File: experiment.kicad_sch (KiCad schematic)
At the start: 4 parts, among them J3 Laser, J4 PZT, U14 MIC94090YC6

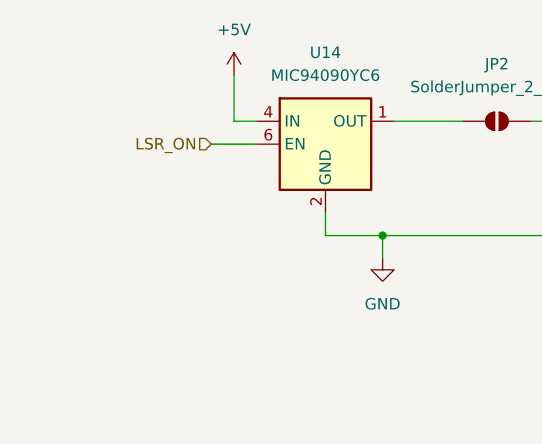
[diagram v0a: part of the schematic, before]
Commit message: Fix review suggestions from non-fpga board
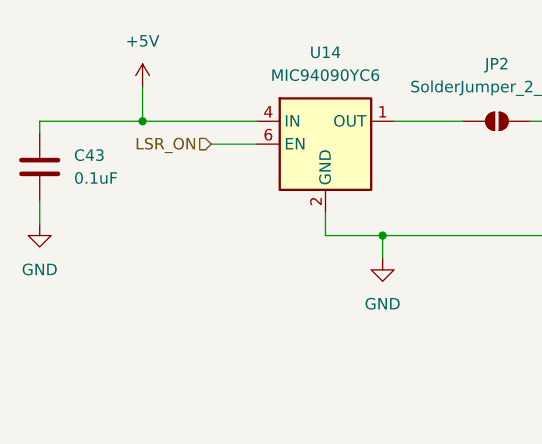
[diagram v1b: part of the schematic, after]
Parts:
- added C43: 0.1uF, Capacitor_SMD:C_0805_2012Metric_Pad1.18x1.45mm_HandSolder, symbol Device:C
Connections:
- net +5V: now also C43.2
- net GND: now also C43.1
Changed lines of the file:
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@@
 	(paper "A4")
+	(junction
+		(at 67.31 64.77)
+		(diameter 0)
+		(color 0 0 0 0)
+	)
 	(junction
 		(at 93.98 77.47)
@@
 	(wire
 		(pts
+			(xy 67.31 60.96) (xy 67.31 64.77)
+		)
+		(stroke
+			(width 0)
+			(type default)
+		)
+	)
+	(wire
+		(pts
 			(xy 96.52 114.3) (xy 96.52 107.95)
 		)
@@
 	(wire
 		(pts
+			(xy 67.31 64.77) (xy 80.01 64.77)
+		)
+		(stroke
+			(width 0)
+			(type default)
+		)
+	)
+	(wire
+		(pts
 			(xy 96.52 107.95) (xy 104.14 107.95)
 		)
@@
 	(wire
 		(pts
+			(xy 55.88 73.66) (xy 55.88 76.2)
+		)
+		(stroke
+			(width 0)
+			(type default)
+		)
+	)
+	(wire
+		(pts
 			(xy 87.63 74.93) (xy 87.63 77.47)
 		)
@@
 	(wire
 		(pts
-			(xy 80.01 64.77) (xy 77.47 64.77)
+			(xy 55.88 64.77) (xy 55.88 66.04)
+		)
+		(stroke
+			(width 0)
+			(type default)
+		)
+	)
+	(wire
+		(pts
+			(xy 55.88 64.77) (xy 67.31 64.77)
 		)
 		(stroke
@@
 		(pts
 			(xy 87.63 77.47) (xy 93.98 77.47)
-		)
-		(stroke
-			(width 0)
-			(type default)
-		)
-	)
-	(wire
-		(pts
-			(xy 77.47 64.77) (xy 77.47 59.69)
 		)
 		(stroke
@@
 	)
 	(symbol
+		(lib_id "power:GND")
+		(at 55.88 76.2 0)
+		(unit 1)
+		(exclude_from_sim no)
+		(in_bom yes)
+		(on_board yes)
+		(dnp no)
+		(fields_autoplaced yes)
+		(property "Reference" "#PWR098"
+			(at 55.88 82.55 0)
+			(effects
+				(font
+					(size 1.27 1.27)
+				)
+				(hide yes)
+			)
+		)
+		(property "Value" "GND"
+			(at 55.88 81.28 0)
+			(effects
+				(font
+					(size 1.27 1.27)
+				)
+			)
+		)
+		(property "Footprint" ""
+			(at 55.88 76.2 0)
+			(effects
+				(font
+					(size 1.27 1.27)
+				)
+				(hide yes)
+			)
+		)
+		(property "Datasheet" ""
+			(at 55.88 76.2 0)
+			(effects
+				(font
+					(size 1.27 1.27)
+				)
+				(hide yes)
+			)
+		)
+		(property "Description" "Power symbol creates a global label with name \"GND\" , ground"
+			(at 55.88 76.2 0)
+			(effects
+				(font
+					(size 1.27 1.27)
+				)
+				(hide yes)
+			)
+		)
+		(pin "1"
+		)
+		(instances
+			(project "FPGA-Lockin"
+				(path "/0d4da0fe-f3e4-47fc-a7f7-d58161fd7b20/40462d7a-51ec-4f16-be35-5e9b22f6b0f0"
+					(reference "#PWR098")
+					(unit 1)
+				)
+			)
+		)
+	)
+	(symbol
+		(lib_id "Device:C")
+		(at 55.88 69.85 180)
+		(unit 1)
+		(exclude_from_sim no)
+		(in_bom yes)
+		(on_board yes)
+		(dnp no)
+		(fields_autoplaced yes)
+		(property "Reference" "C43"
+			(at 59.69 68.5799 0)
+			(effects
+				(font
+					(size 1.27 1.27)
+				)
+				(justify right)
+			)
+		)
+		(property "Value" "0.1uF"
+			(at 59.69 71.1199 0)
+			(effects
+				(font
+					(size 1.27 1.27)
+				)
+				(justify right)
+			)
+		)
+		(property "Footprint" "Capacitor_SMD:C_0805_2012Metric_Pad1.18x1.45mm_HandSolder"
+			(at 54.9148 66.04 0)
+			(effects
+				(font
+					(size 1.27 1.27)
+				)
+				(hide yes)
+			)
+		)
+		(property "Datasheet" "~"
+			(at 55.88 69.85 0)
+			(effects
+				(font
+					(size 1.27 1.27)
+				)
+				(hide yes)
+			)
+		)
+		(property "Description" "Unpolarized capacitor"
+			(at 55.88 69.85 0)
+			(effects
+				(font
+					(size 1.27 1.27)
+				)
+				(hide yes)
+			)
+		)
+		(pin "2"
+		)
+		(pin "1"
+		)
+		(instances
+			(project ""
+				(path "/0d4da0fe-f3e4-47fc-a7f7-d58161fd7b20/40462d7a-51ec-4f16-be35-5e9b22f6b0f0"
+					(reference "C43")
+					(unit 1)
+				)
+			)
+		)
+	)
+	(symbol
 		(lib_id "power:+5V")
-		(at 77.47 59.69 0)
+		(at 67.31 60.96 0)
 		(unit 1)
 		(exclude_from_sim no)
@@
 		(fields_autoplaced yes)
 		(property "Reference" "#PWR067"
-			(at 77.47 63.5 0)
+			(at 67.31 64.77 0)
 			(effects
 				(font
@@
 		)
 		(property "Value" "+5V"
-			(at 77.47 54.61 0)
+			(at 67.31 55.88 0)
 			(effects
 				(font
@@
 		)
 		(property "Footprint" ""
-			(at 77.47 59.69 0)
+			(at 67.31 60.96 0)
 			(effects
 				(font
@@
 		)
 		(property "Datasheet" ""
-			(at 77.47 59.69 0)
+			(at 67.31 60.96 0)
 			(effects
 				(font
@@
 		)
 		(property "Description" "Power symbol creates a global label with name \"+5V\""
-			(at 77.47 59.69 0)
-			(effects
-				(font
+			(at 67.31 60.96 0)
+			(effects
+				(font

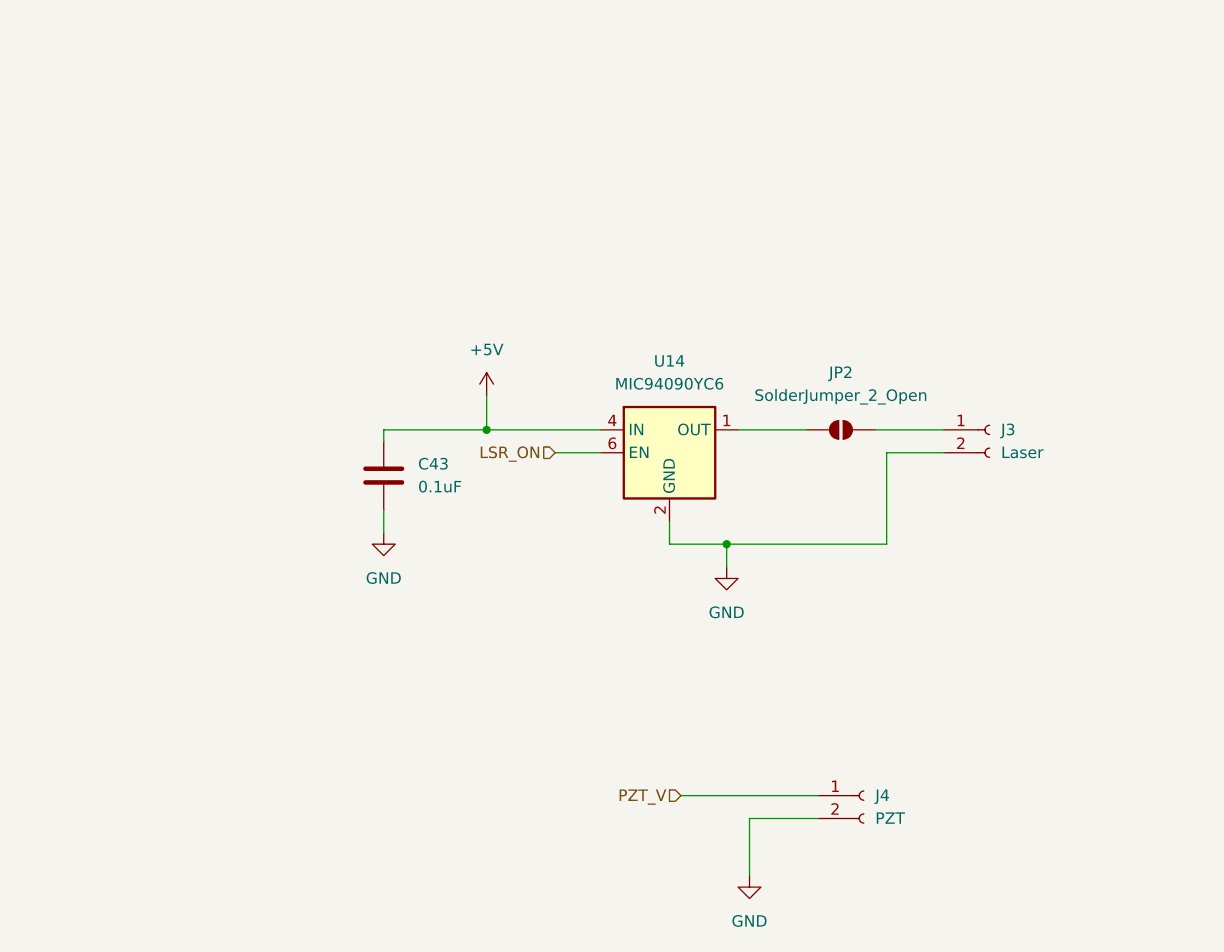
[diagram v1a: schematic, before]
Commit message: Fix everything based on component availabilty
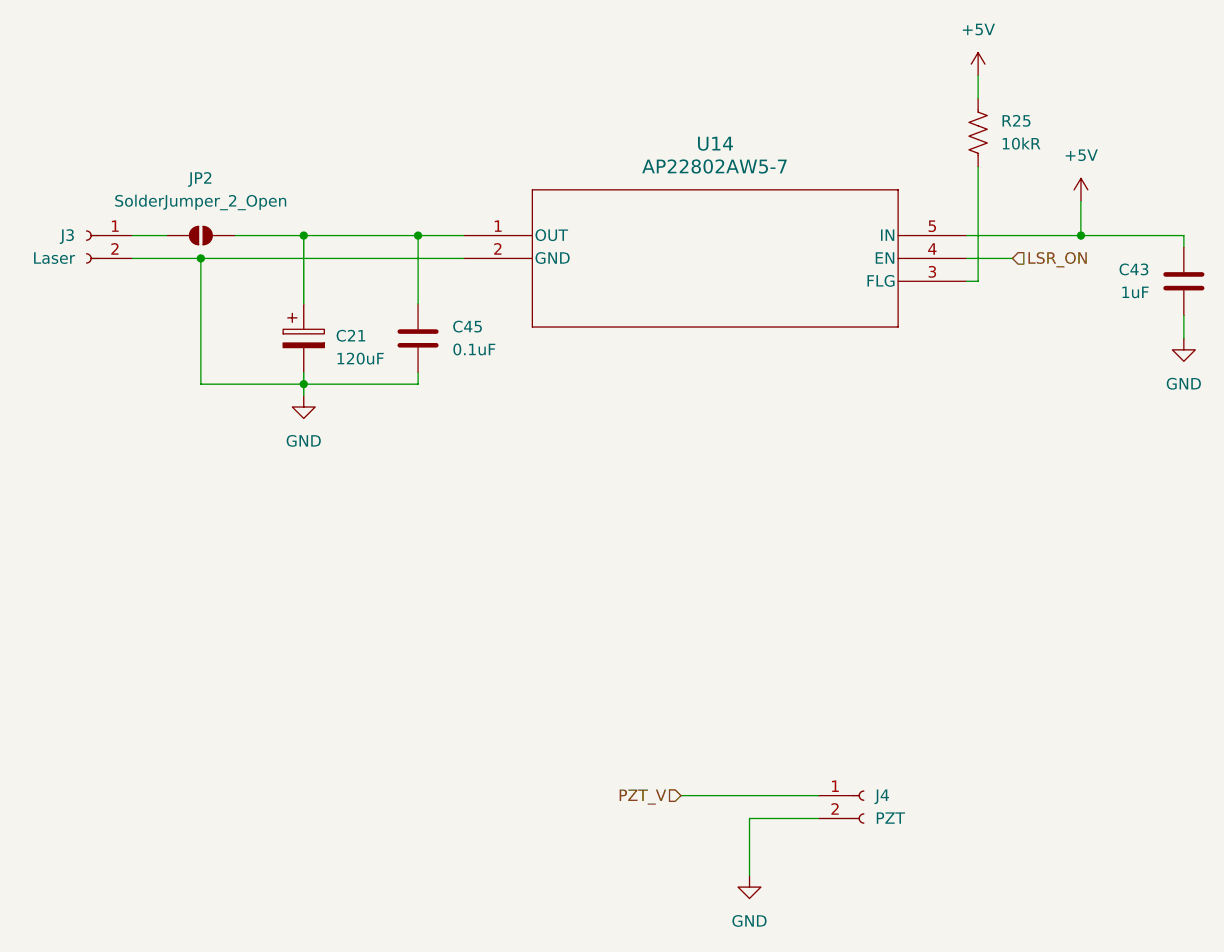
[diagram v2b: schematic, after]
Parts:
- removed U14: MIC94090YC6, Package_TO_SOT_SMD:SOT-363_SC-70-6, symbol Power_Management:MIC94090YC6
- added C21: 120uF, Capacitor_Tantalum_SMD:CP_EIA-7132-20_AVX-U_HandSolder, symbol Device:C_Polarized
- added C45: 0.1uF, Capacitor_SMD:C_0805_2012Metric_Pad1.18x1.45mm_HandSolder, symbol Device:C
- added R25: 10kR, Resistor_SMD:R_0805_2012Metric_Pad1.20x1.40mm_HandSolder, symbol Device:R_US
- added U14: AP22802AW5-7, switch:SOT25_DIO, symbol switch:AP22802AW5-7
- C43: value 0.1uF -> 1uF
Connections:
- net +5V: now also R25.1, U14.5 (IN)
- net GND: now also C21.2, C45.2, U14.2 (GND)
- net LSR_ON: now also U14.4 (EN)
- net at JP2.1 (A): now also C21.1, C45.1, U14.1 (OUT)
- new net: R25.2, U14.3 (FLG)
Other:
- moved on the sheet: C43, J3, JP2
